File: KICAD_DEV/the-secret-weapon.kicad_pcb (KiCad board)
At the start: 6 copper layers, 150 x 150 mm, 0 parts

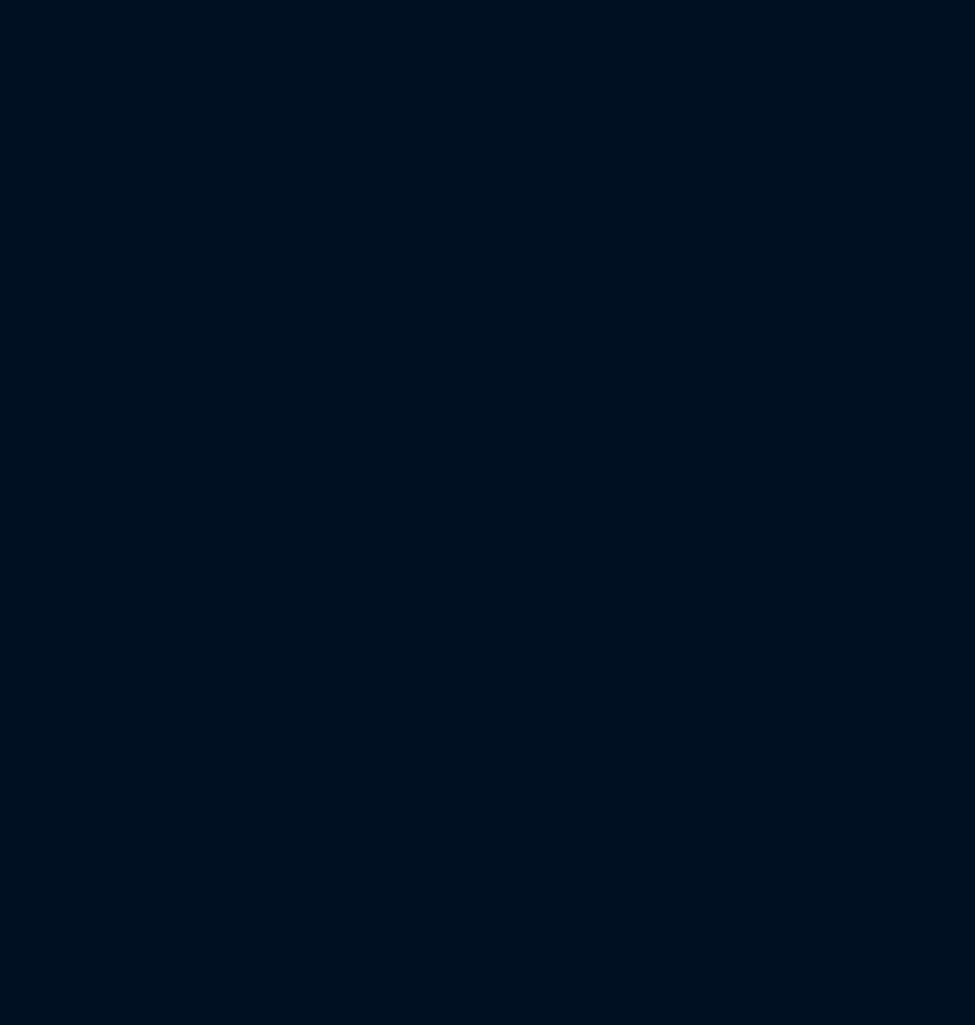
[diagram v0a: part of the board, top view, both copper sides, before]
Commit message: ground pour + core SoC STM32H757
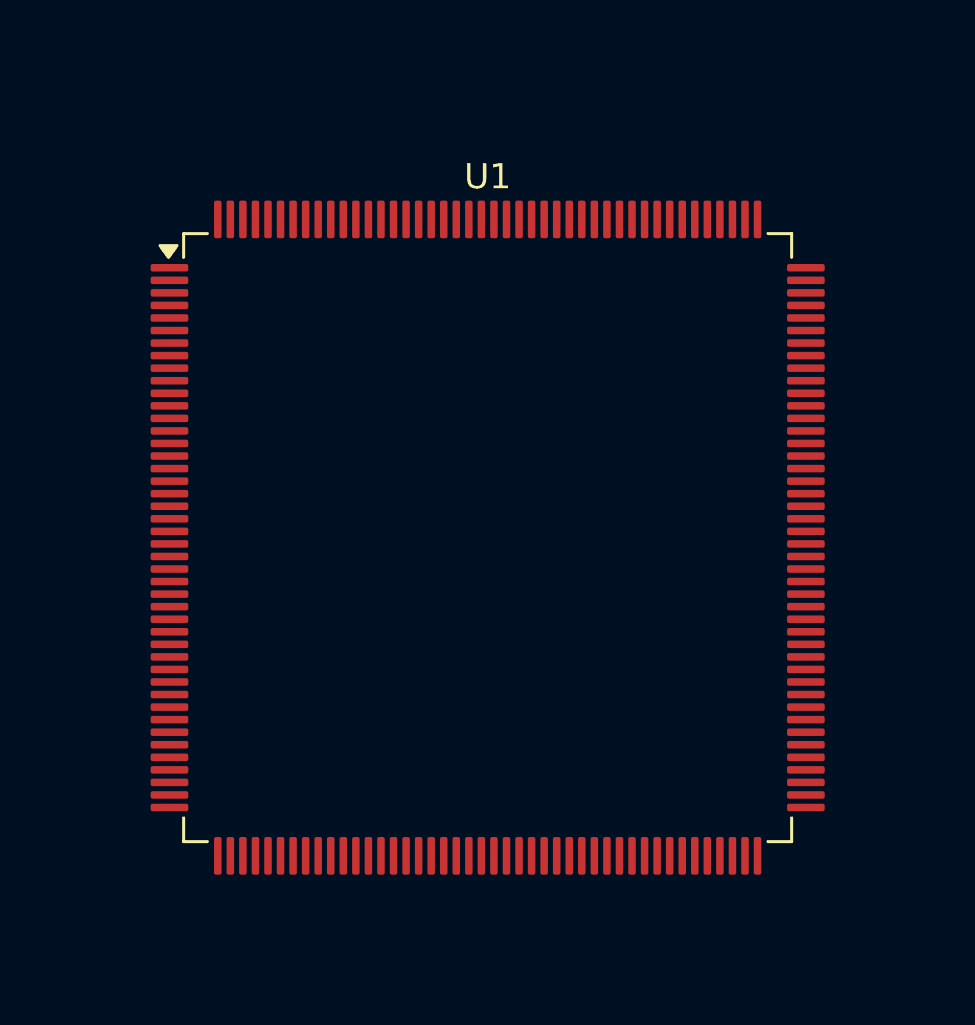
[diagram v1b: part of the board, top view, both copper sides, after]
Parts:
- added U1: STM32H7A3IGTx, Package_QFP:LQFP-176_24x24mm_P0.5mm, F.Cu at (150.0, 70.5)
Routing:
- added copper zone on In1.Cu, net GND
- added copper zone on In4.Cu, net GND

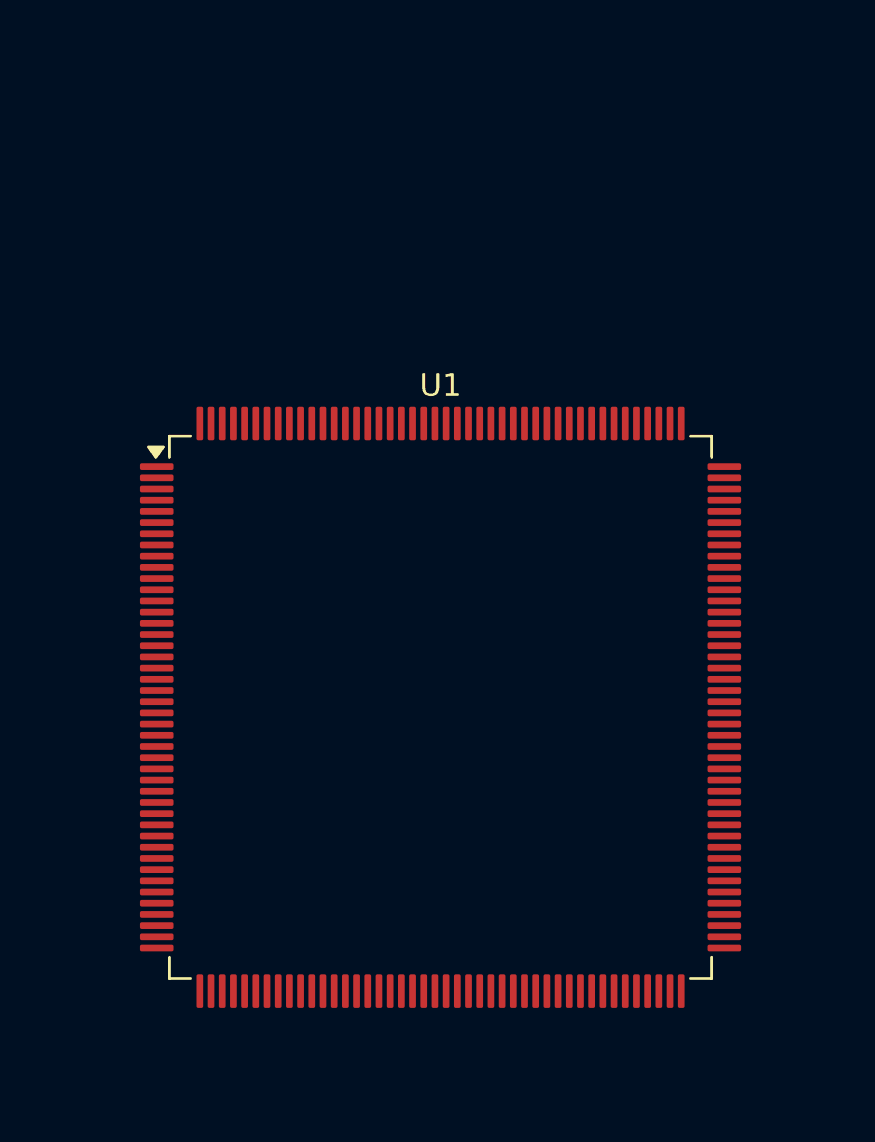
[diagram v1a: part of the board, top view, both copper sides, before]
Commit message: accidently used the wrong symbol
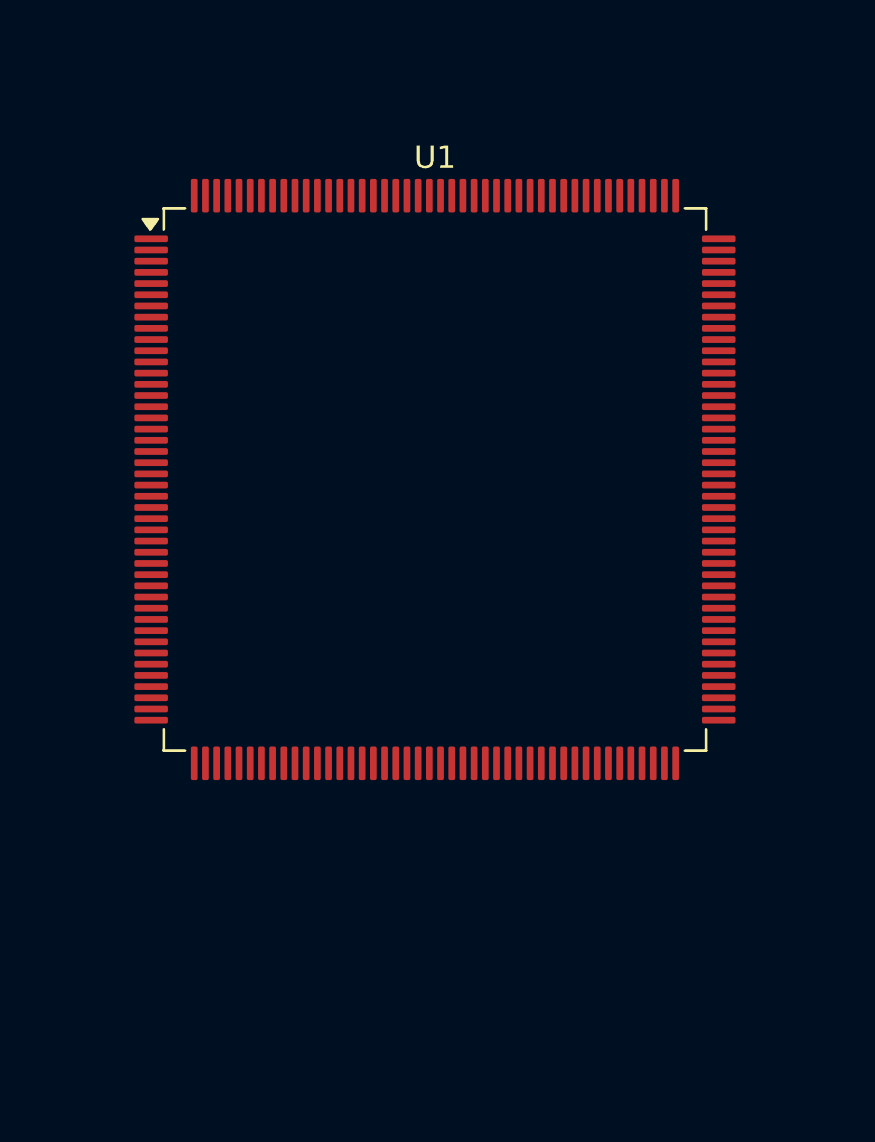
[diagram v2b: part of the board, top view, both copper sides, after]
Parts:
- U1: value STM32H7A3IGTx -> STM32H757IITx
- moved U1 10.2 mm to (149.8, 60.3)
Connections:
- U1 pad 100: unconnected-(U1-PD12-Pad100) -> GND
- U1 pad 101: unconnected-(U1-PD13-Pad101) -> Net-(U1-VCAPDSI)
- U1 pad 102: GND -> unconnected-(U1-VDD12DSI-Pad102)
- U1 pad 105: unconnected-(U1-PD15-Pad105) -> GND
- U1 pad 109: unconnected-(U1-PG5-Pad109) -> GND
- U1 pad 112: unconnected-(U1-PG8-Pad112) -> GND
- U1 pad 113: GND -> unconnected-(U1-VDD-Pad113)
- U1 pad 119: unconnected-(U1-PA8-Pad119) -> GND
- U1 pad 12: unconnected-(U1-PI10-Pad12) -> GND
- U1 pad 126: GND -> unconnected-(U1-VDD-Pad126)
- U1 pad 133: unconnected-(U1-PI2-Pad133) -> Net-(C8-Pad2)
- U1 pad 134: unconnected-(U1-PI3-Pad134) -> GND
- U1 pad 135: GND -> unconnected-(U1-VDDLDO-Pad135)
- U1 pad 137: unconnected-(U1-PA14-Pad137) -> GND
- U1 pad 148: GND -> unconnected-(U1-PD5-Pad148)
- U1 pad 151: unconnected-(U1-PD7-Pad151) -> GND
- U1 pad 158: GND -> unconnected-(U1-PG14-Pad158)
- U1 pad 159: unconnected-(U1-VDD-Pad159) -> GND
- U1 pad 172: unconnected-(U1-VDD-Pad172) -> Net-(C9-Pad2)
- U1 pad 173: unconnected-(U1-PI4-Pad173) -> GND
- U1 pad 22: GND -> unconnected-(U1-PF4-Pad22)
- U1 pad 24: unconnected-(U1-PF6-Pad24) -> GND
- U1 pad 37: GND -> unconnected-(U1-PC3_C-Pad37)
- U1 pad 38: unconnected-(U1-VREF+-Pad38) -> GND
- U1 pad 45: unconnected-(U1-PH4-Pad45) -> GND
- U1 pad 47: unconnected-(U1-PA3-Pad47) -> GND
- U1 pad 48: GND -> unconnected-(U1-VDD-Pad48)
- U1 pad 6: unconnected-(U1-VBAT-Pad6) -> GND
- U1 pad 61: GND -> unconnected-(U1-PF14-Pad61)
- U1 pad 64: unconnected-(U1-PF14-Pad64) -> GND
- U1 pad 70: unconnected-(U1-PE9-Pad70) -> GND
- U1 pad 71: GND -> unconnected-(U1-VDD-Pad71)
- U1 pad 80: unconnected-(U1-PB11-Pad80) -> Net-(C7-Pad2)
- U1 pad 81: unconnected-(U1-VCAP-Pad81) -> GND
- U1 pad 83: unconnected-(U1-PH6-Pad83) -> GND
- U1 pad 90: GND -> unconnected-(U1-PD9-Pad90)
- U1 pad 93: unconnected-(U1-PB13-Pad93) -> GND

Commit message: updating some stuff
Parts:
- added U2: TPS26750, Package_DFN_QFN:VQFN-32-1EP_4x4mm_P0.4mm_EP2.8x2.8mm_ThermalVias, F.Cu at (124.0, 55.9)
- added U3: TPD4S480, Package_DFN_QFN:WQFN-20-1EP_3x3mm_P0.4mm_EP1.7x1.7mm_ThermalVias, F.Cu at (123.5, 61.7)
- U1: value STM32H757IITx -> STM32H743VITx; footprint Package_QFP:LQFP-176_24x24mm_P0.5mm -> Package_QFP:LQFP-100_14x14mm_P0.5mm
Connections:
- U1 pad 10: unconnected-(U1-PC14-Pad10) -> GND
- U1 pad 100: GND -> +3V3
- U1 pad 11: unconnected-(U1-PC15-Pad11) -> +3V3
- U1 pad 12: GND -> unconnected-(U1-PH0-Pad12)
- U1 pad 14: GND -> RESET
- U1 pad 19: unconnected-(U1-PF1-Pad19) -> GND
- U1 pad 20: unconnected-(U1-PF2-Pad20) -> +3V3
- U1 pad 21: unconnected-(U1-PF3-Pad21) -> +3V3
- U1 pad 24: GND -> unconnected-(U1-PA2-Pad24)
- U1 pad 26: unconnected-(U1-PF6-Pad26) -> GND
- U1 pad 27: unconnected-(U1-PF7-Pad27) -> +3V3
- U1 pad 38: GND -> unconnected-(U1-PE8-Pad38)
- U1 pad 45: GND -> unconnected-(U1-PE15-Pad45)
- U1 pad 47: GND -> unconnected-(U1-PB11-Pad47)
- U1 pad 48: unconnected-(U1-VDD-Pad48) -> Net-(C7-Pad1)
- U1 pad 49: unconnected-(U1-PA4-Pad49) -> GND
- U1 pad 50: unconnected-(U1-PA5-Pad50) -> +3V3
- U1 pad 6: GND -> unconnected-(U1-VBAT-Pad6)
- U1 pad 64: GND -> unconnected-(U1-PC7-Pad64)
- U1 pad 70: GND -> unconnected-(U1-PA11-Pad70)
- U1 pad 73: unconnected-(U1-PE11-Pad73) -> Net-(C7-Pad1)
- U1 pad 74: unconnected-(U1-PE12-Pad74) -> GND
- U1 pad 75: unconnected-(U1-PE13-Pad75) -> +3V3
- U1 pad 80: Net-(C7-Pad2) -> unconnected-(U1-PC12-Pad80)
- U1 pad 81: GND -> unconnected-(U1-PD0-Pad81)
- U1 pad 83: GND -> unconnected-(U1-PD2-Pad83)
- U1 pad 93: GND -> unconnected-(U1-PB7-Pad93)
- U1 pad 94: unconnected-(U1-PD11-Pad94) -> Net-(U1-BOOT0)
- U1 pad 99: unconnected-(U1-VDD-Pad99) -> GND

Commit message: some more progress
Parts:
- removed U3: TPD4S480, Package_DFN_QFN:WQFN-20-1EP_3x3mm_P0.4mm_EP1.7x1.7mm_ThermalVias
- U2: value TPS26750 -> USBLC6-2SC6; footprint Package_DFN_QFN:VQFN-32-1EP_4x4mm_P0.4mm_EP2.8x2.8mm_ThermalVias -> Package_TO_SOT_SMD:SOT-23-6
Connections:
- net ADCIN1 renamed USB_D+
- net LDO_1V5 renamed D+
- net Net-(U1-BOOT0) renamed BOOT
- U1 pad 12: unconnected-(U1-PH0-Pad12) -> OSC_IN
- U1 pad 13: unconnected-(U1-PH1-Pad13) -> OSC_OUT
- U1 pad 8: unconnected-(U1-PC14-Pad8) -> OSC32_IN
- U1 pad 9: unconnected-(U1-PC15-Pad9) -> OSC32_OUT
- U2 pad 1: LDO_3V3 -> USB_D-
- U2 pad 2: ADCIN2 -> GND
- U2 pad 5: unconnected-(U2-GPIO0-Pad5) -> +5V
- U2 pad 6: unconnected-(U2-GPIO1-Pad6) -> D-

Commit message: starting the actual board!
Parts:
- added C1: 100uF, Capacitor_SMD:C_Elec_8x6.2, F.Cu at (103.2, 91.0)
- added C10: 0.1uF, Capacitor_SMD:C_0402_1005Metric, F.Cu at (116.4, 70.6)
- added C11: 22uF, Capacitor_SMD:C_0805_2012Metric, F.Cu at (83.1, 81.2)
- added C12: 22uF, Capacitor_SMD:C_0805_2012Metric, F.Cu at (83.1, 84.2)
- added C13: 1uF, Capacitor_SMD:C_0402_1005Metric, F.Cu at (82.3, 96.7)
- added C14: 10uF, Capacitor_SMD:C_0805_2012Metric, F.Cu at (83.1, 87.2)
- added C15: 22uF, Capacitor_SMD:C_0805_2012Metric, F.Cu at (83.1, 90.2)
- added C2: 220nF, Capacitor_SMD:C_0402_1005Metric, F.Cu at (82.3, 92.7)
- added C21: 0.1uF, Capacitor_SMD:C_0402_1005Metric, F.Cu at (116.4, 72.5)
- added C23: 0.1uF, Capacitor_SMD:C_0402_1005Metric, F.Cu at (116.4, 74.5)
- added C24: 0.1uF, Capacitor_SMD:C_0402_1005Metric, F.Cu at (119.3, 66.6)
- added C25: 0.1uF, Capacitor_SMD:C_0402_1005Metric, F.Cu at (119.3, 68.6)
- added C26: 0.1uF, Capacitor_SMD:C_0402_1005Metric, F.Cu at (119.3, 70.6)
- added C27: 0.1uF, Capacitor_SMD:C_0402_1005Metric, F.Cu at (119.3, 72.5)
- added C28: 32pF, Capacitor_SMD:C_0402_1005Metric, F.Cu at (119.3, 74.5)
- added C29: 32pF, Capacitor_SMD:C_0402_1005Metric, F.Cu at (122.2, 66.6)
- added C3: 10uF, Capacitor_SMD:C_0603_1608Metric, F.Cu at (105.0, 83.1)
- added C30: 17pF, Capacitor_SMD:C_0402_1005Metric, F.Cu at (122.2, 68.6)
- added C31: 17pF, Capacitor_SMD:C_0402_1005Metric, F.Cu at (122.2, 70.6)
- added C4: 0.1uF, Capacitor_SMD:C_0402_1005Metric, F.Cu at (82.3, 94.7)
- added C5: 22uF, Capacitor_SMD:C_0805_2012Metric, F.Cu at (83.1, 75.2)
- added C6: 22uF, Capacitor_SMD:C_0805_2012Metric, F.Cu at (83.1, 78.2)
- added C7: 2.2uF, Capacitor_SMD:C_0402_1005Metric, F.Cu at (116.4, 66.6)
- added C8: 2.2uF, Capacitor_SMD:C_0402_1005Metric, F.Cu at (116.4, 68.6)
- added C9: 4.7uF, Capacitor_SMD:C_0603_1608Metric, F.Cu at (117.0, 80.1)
- added F1: 20A, Fuse:FuseHolder_Blade_ATO_Littelfuse_FLR_178.6165, F.Cu at (85.5, 68.4)
- added J1: USB_C_Receptacle_USB2.0_14P, Connector_USB:USB_C_Receptacle_HRO_TYPE-C-31-M-12, F.Cu at (120.7, 89.5)
- added J2: Screw_Terminal_01x02, TerminalBlock_Phoenix:TerminalBlock_Phoenix_PT-1,5-2-5.0-H_1x02_P5.00mm_Horizontal, F.Cu at (88.9, 91.1)
- added L1: 6.8uH, Inductor_SMD:L_TechFuse_SL0650, F.Cu at (108.0, 77.8)
- added R1: 5.1K, Resistor_SMD:R_0402_1005Metric, F.Cu at (110.5, 87.0)
- added R13: 10K, Resistor_SMD:R_0402_1005Metric, F.Cu at (121.5, 76.5)
- added R14: 10K, Resistor_SMD:R_0402_1005Metric, F.Cu at (121.5, 78.5)
- added R2: 5.1K, Resistor_SMD:R_0402_1005Metric, F.Cu at (110.5, 89.0)
- added R3: 100K, Resistor_SMD:R_0402_1005Metric, F.Cu at (110.5, 91.0)
- added R4: 24.9K, Resistor_SMD:R_0402_1005Metric, F.Cu at (110.5, 93.0)
- added SW1: SW_Push, Button_Switch_SMD:SW_Push_SPST_NO_Alps_SKRK, F.Cu at (126.9, 67.9)
- added SW2: SW_Push, Button_Switch_SMD:SW_Push_SPST_NO_Alps_SKRK, F.Cu at (126.9, 72.3)
- added U3: LMR33640ADDA, Package_SO:Texas_HSOP-8-1EP_3.9x4.9mm_P1.27mm_ThermalVias, F.Cu at (107.2, 69.0)
- added U4: LM1086S-3.3/TR, Package_TO_SOT_SMD:TO-263-3_TabPin2, F.Cu at (96.1, 79.9)
- added Y1: 8 MHz, Crystal:Crystal_SMD_TXC_7A-2Pin_5x3.2mm, F.Cu at (127.1, 76.9)
- added Y2: 32.768 KHz, Crystal:Crystal_SMD_3215-2Pin_3.2x1.5mm, F.Cu at (117.5, 77.2)

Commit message: starting the layout of my power system!
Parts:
- moved F1 127.1 mm to (167.5, 165.6), turned to 180 degrees
- moved U3 111.7 mm to (147.9, 173.0), turned to 180 degrees
- moved J2 110.9 mm to (163.6, 172.9)
- moved L1 101.1 mm to (139.6, 173.8), turned to 180 degrees
- moved C1 97.7 mm to (156.1, 173.1), turned to -90 degrees
- moved U4 97.4 mm to (144.1, 164.6)
- moved J1 86.6 mm to (129.8, 175.5)
- moved U1 46.1 mm to (160.0, 105.2), turned to 90 degrees

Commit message: an absolutely gorgeous power layoutgit add .
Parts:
- moved C6 111.1 mm to (133.5, 177.2), turned to 180 degrees
- moved U2 110.1 mm to (125.9, 166.0), turned to 90 degrees
- moved C5 108.2 mm to (133.5, 171.0), turned to 180 degrees
- moved C11 104.4 mm to (132.8, 173.0), turned to 180 degrees
- moved C2 103.7 mm to (150.7, 170.6), turned to 180 degrees
- moved C12 103.6 mm to (132.8, 175.1), turned to 180 degrees
- moved C4 103.5 mm to (144.7, 177.3), turned to 180 degrees
- moved C3 97.3 mm to (150.1, 169.3), turned to 180 degrees
- moved C13 96.3 mm to (143.5, 171.0), turned to 90 degrees
- moved C14 92.3 mm to (130.0, 166.7), turned to 180 degrees
- moved C15 87.5 mm to (130.0, 164.2), turned to 180 degrees
- moved R3 86.8 mm to (145.1, 170.6)
- moved R4 85.8 mm to (147.0, 170.6)
- moved R1 83.4 mm to (124.4, 169.3), turned to 90 degrees
- moved R2 82.1 mm to (127.4, 169.3), turned to 90 degrees
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
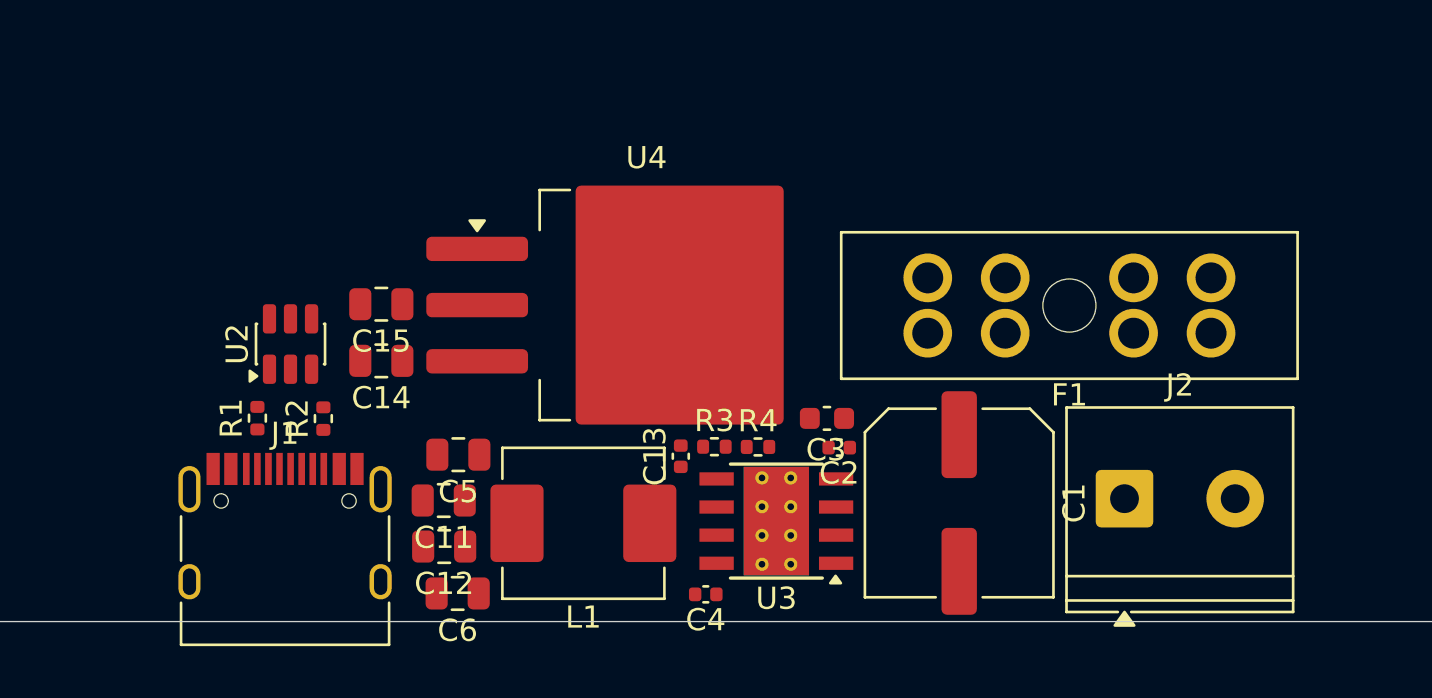
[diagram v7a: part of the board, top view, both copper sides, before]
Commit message: changing cap size, but it's probably not adequate
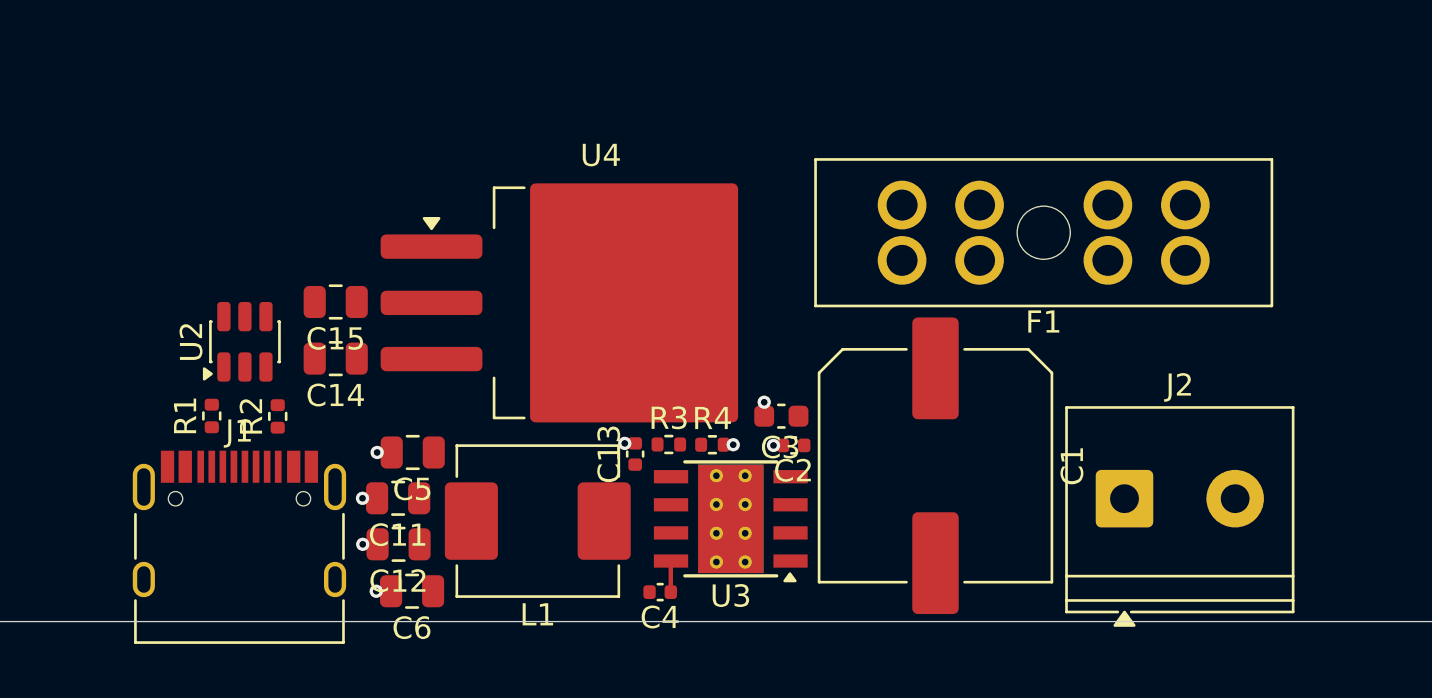
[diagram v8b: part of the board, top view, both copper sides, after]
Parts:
- C1: value 100uF -> 1000uF; footprint Capacitor_SMD:C_Elec_8x6.2 -> Capacitor_SMD:C_Elec_10x10.2
- moved F1 3.49 mm to (166.3, 162.2)
- moved C12 2.06 mm to (130.8, 175.0)
- moved R2 2.06 mm to (125.3, 169.2)
- moved R4 2.06 mm to (145.0, 170.5)
- moved C11 2.06 mm to (130.8, 172.9)
- moved C13 2.06 mm to (141.5, 170.9)
- moved C2 2.06 mm to (148.6, 170.5)
- moved C3 2.06 mm to (148.1, 169.2)
- moved C5 2.06 mm to (131.4, 170.9)
- moved C6 2.06 mm to (131.4, 177.1)
- moved J1 2.06 mm to (123.6, 175.6)
- moved R1 2.06 mm to (122.3, 169.2)
- moved R3 2.06 mm to (143.0, 170.5)
- moved U2 2.06 mm to (123.8, 165.9)
- moved U3 2.06 mm to (145.8, 173.9)
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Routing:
- net GND: track 0.00 -> 4.62 mm, vias 0 -> 8
- net Net-(U3-SW): track 0.00 -> 1.41 mm
